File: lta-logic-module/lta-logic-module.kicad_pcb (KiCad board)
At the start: 2 copper layers, 125 x 89.5 mm, 104 parts, among them J1 Molex-MicroFit_43650-0218, J2 Molex-MicroLatch-53253-1270, J3 Molex-MicroLatch-53253-1270, J4 Molex-MicroLatch-53253-1270, Q1 PT334-6B, Q2 2N3904, SW1 SW_SPST, U1 Feather_M4_Express, U10 SN74LVC00AD, U11 SN74LVC14AD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

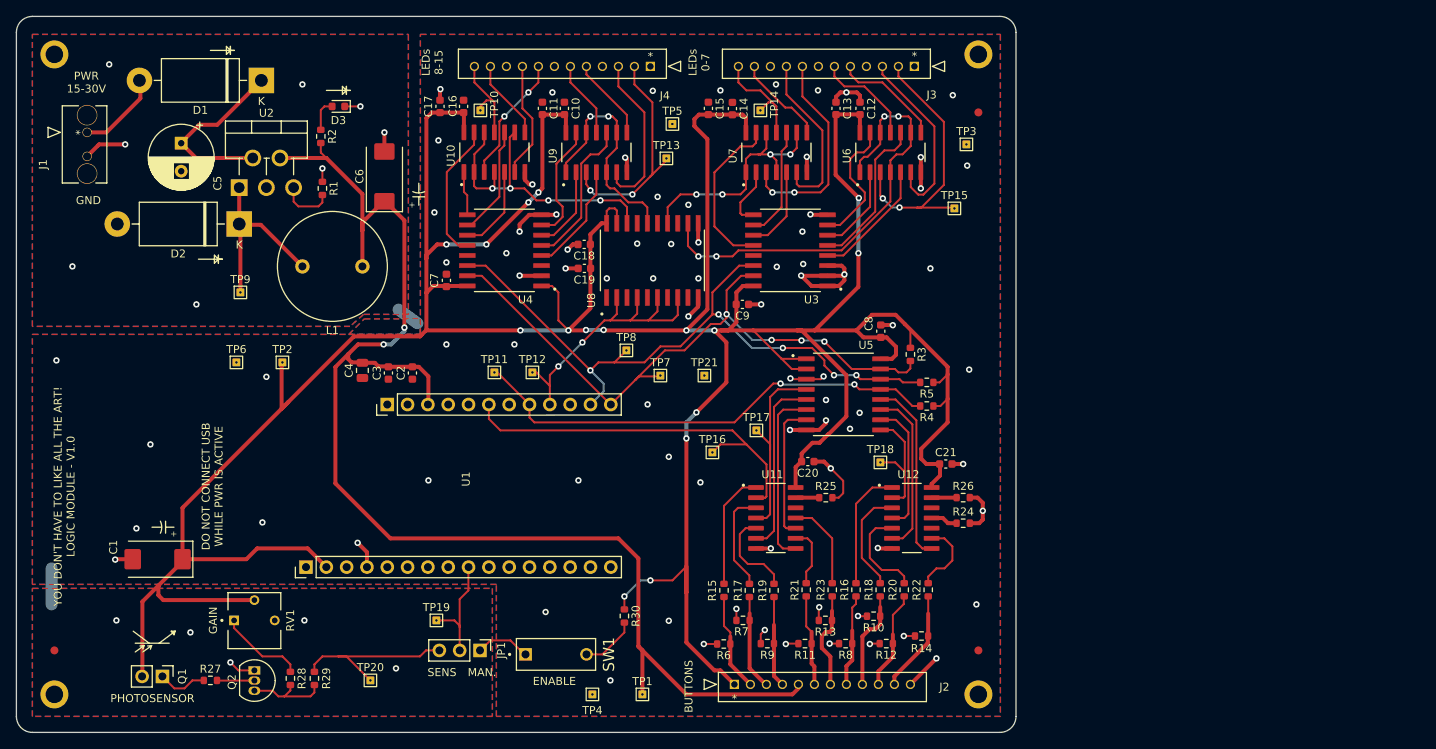
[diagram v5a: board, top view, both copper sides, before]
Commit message: Add indicator LED to SW1 enabled.
Adds 220K pull-down resistor to DARK signal. (Validated.)
Update solder thief pads and process direction indicator.
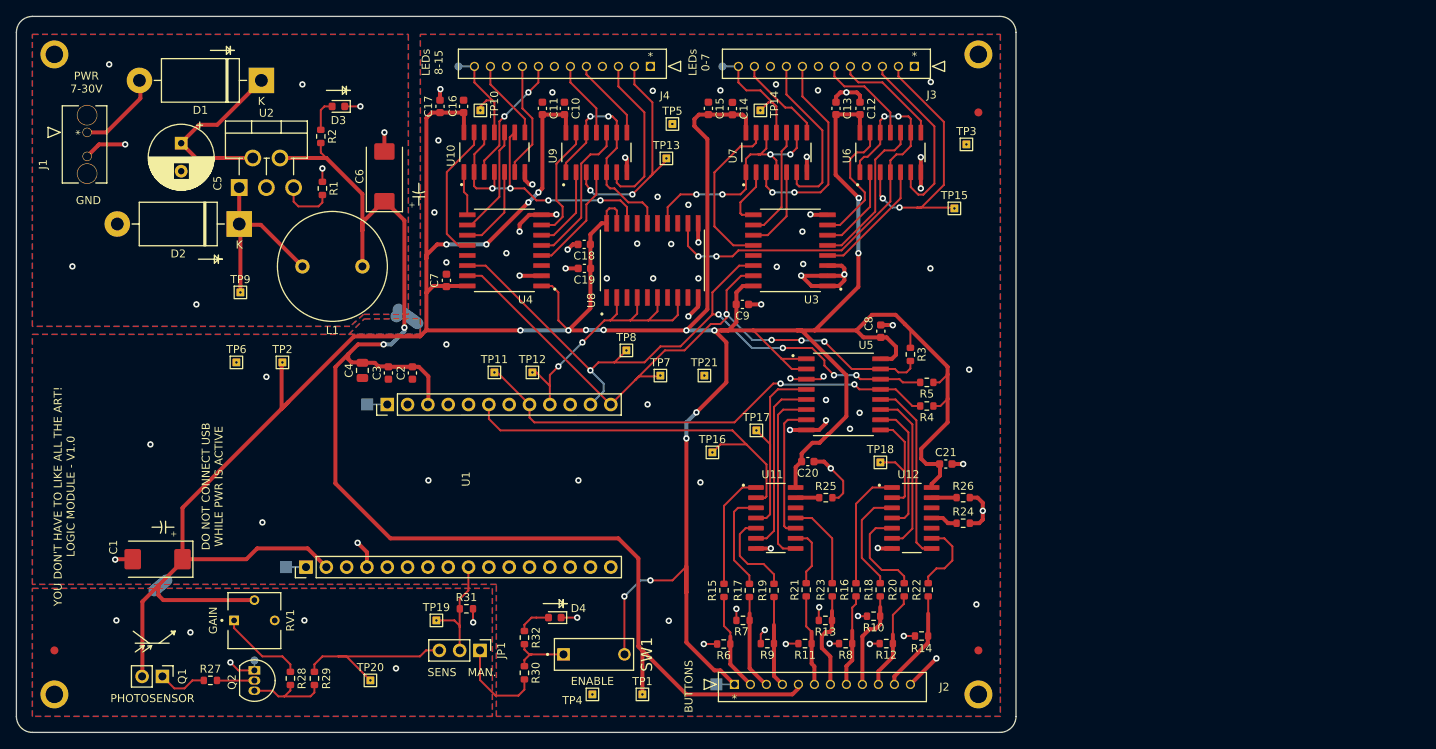
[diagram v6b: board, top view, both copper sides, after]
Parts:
- added D4: DARK_EN, LED_SMD:LED_0603_1608Metric, F.Cu at (84.3, 92.7)
- added R31: 220K, Resistor_SMD:R_0603_1608Metric, F.Cu at (73.3, 91.5)
- added R32: 120R, Resistor_SMD:R_0603_1608Metric, F.Cu at (80.5, 95.2)
- added TP22: Thief, Aaron_Pads:Pad_1.5x1.5mm, B.Cu at (50.8, 86.3)
- added TP23: Thief, Aaron_Pads:Pad_1.5x1.5mm, B.Cu at (60.9, 66.0)
- added TP24: Thief, Aaron_Pads:Pad_D1.0mm, B.Cu at (105.3, 23.8)
- added TP25: Thief, Aaron_Pads:Pad_D1.0mm, B.Cu at (72.3, 23.8)
- added TP26: Thief, Aaron_Pads:Pad_1.5x1.5mm, B.Cu at (104.5, 101.0)
- added TP27: Thief, Aaron_Pads:Pad_D1.0mm, B.Cu at (46.8, 98.0)
- J2, J3, J4: value Molex-MicroLatch-53253-1270 -> Molex-MicroLatch_53253-1270
- moved R30 14.4 mm to (80.5, 99.5)
- moved SW1 4.75 mm to (89.2, 97.2)
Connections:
- R30 pad 1: +3V3 -> Net-(SW1-Pad1)
- R30 pad 2: Net-(R30-Pad2) -> Net-(JP1-Pad1)
- SW1 pad 1: Net-(JP1-Pad1) -> Net-(SW1-Pad1)
- SW1 pad 2: Net-(R30-Pad2) -> +3V3
- U1 pad 1: unconnected-(U1-Pad1) -> Net-(TP22-Pad1)
- U1 pad 28: unconnected-(U1-Pad28) -> Net-(TP23-Pad1)
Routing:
- net +3V3: track 489.0 -> 497.0 mm
- net Net-(SW1-Pad1): track 0.00 -> 7.78 mm
- net Net-(R30-Pad2): track 7.10 -> 0.00 mm
- net Net-(JP1-Pad1): track 7.10 -> 11.7 mm
- net Net-(D4-Pad2): track 0.00 -> 4.16 mm
- net GND: track 128.1 -> 131.4 mm, vias 95 -> 90
- net Net-(TP22-Pad1): track 0.00 -> 2.64 mm
- net Net-(TP23-Pad1): track 0.00 -> 2.50 mm
- net /LED Signal Outputs/s7: track 13.2 -> 15.2 mm
- net /LED Signal Outputs/s15: track 11.6 -> 13.1 mm
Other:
- board text added: "<<< WAVE PROCESS DIRECTION <<<"
- board text added: "PWR 7-30V"
- board text removed: "PWR 15-30V"

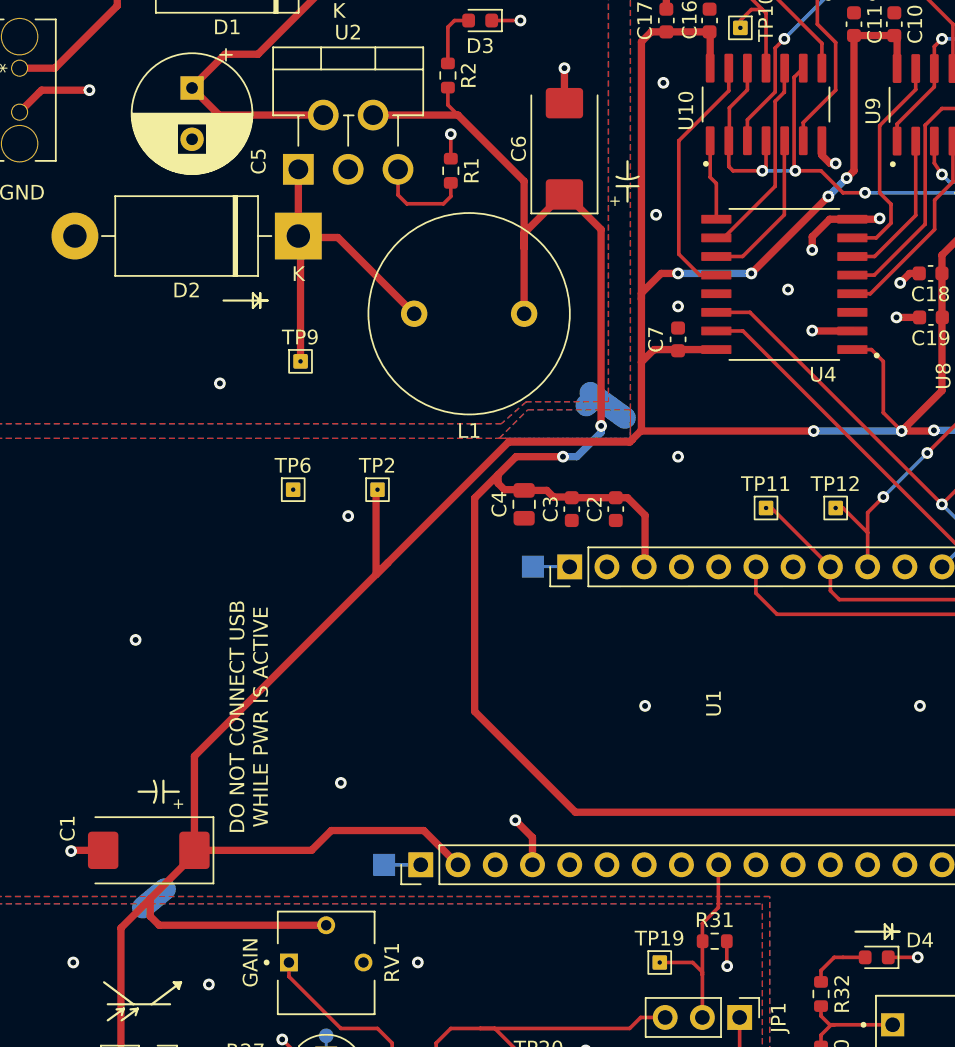
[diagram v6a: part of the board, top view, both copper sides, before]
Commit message: Generate logic module 2022-05-08 v1.0 fab documentation.
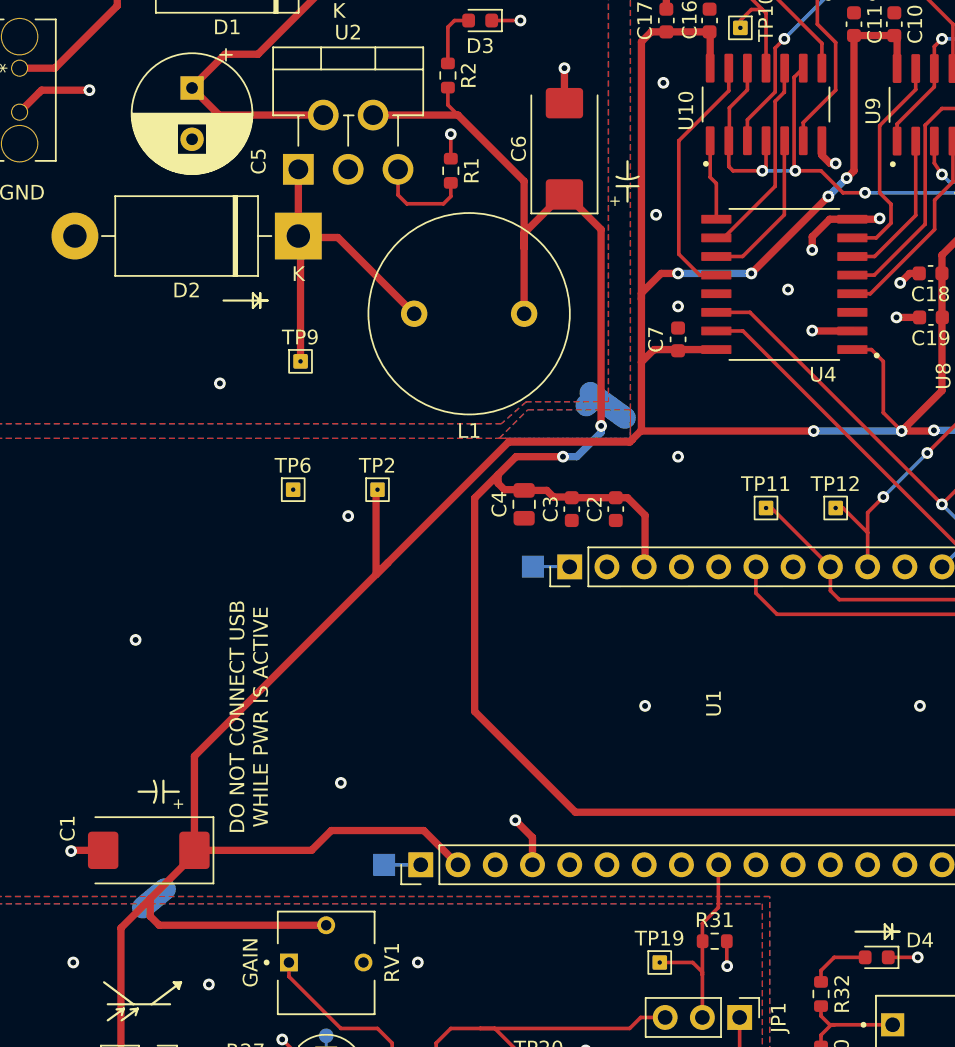
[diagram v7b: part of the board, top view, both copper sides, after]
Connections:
- net /BUTTON_INT_L renamed /~{BUTTON_INT_L}
